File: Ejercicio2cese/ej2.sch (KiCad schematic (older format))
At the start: 2 parts

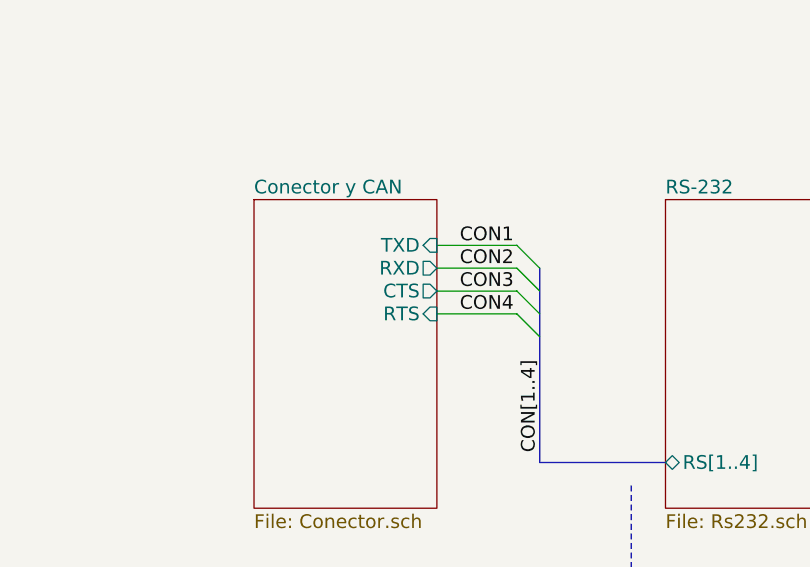
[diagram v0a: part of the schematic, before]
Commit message: Agrego RS232 multipart al esquemático. Cambio nombres de líneas seriales.
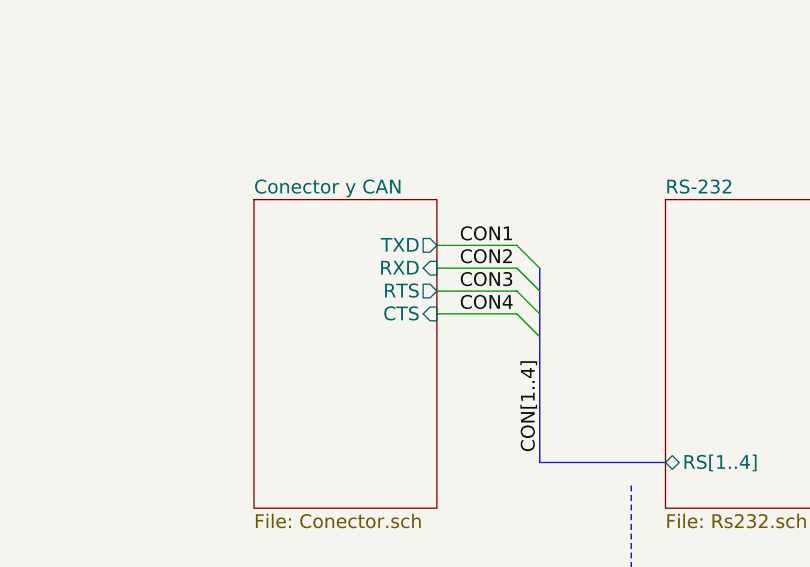
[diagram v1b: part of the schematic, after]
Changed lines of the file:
@@
 LIBS:power
 LIBS:fiducial
+LIBS:max232_mp
 LIBS:ej2-cache
 EELAYER 25 0
@@
 F0 "Conector y CAN" 60
 F1 "Conector.sch" 60
-F2 "TXD" I R 5300 3100 60
-F3 "RXD" O R 5300 3200 60
-F4 "RTS" I R 5300 3400 60
-F5 "CTS" O R 5300 3300 60
+F2 "TXD" O R 5300 3100 60
+F3 "RXD" I R 5300 3200 60
+F4 "RTS" O R 5300 3300 60
+F5 "CTS" I R 5300 3400 60
 $EndSheet
 $Sheet
